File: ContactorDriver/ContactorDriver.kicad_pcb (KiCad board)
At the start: 2 copper layers, 66 x 100 mm, 40 parts, among them J1 PowerConn, J2 DashboardConn, J3 DashboardConn, J4 ContactorConn, J5 PrechargeConn, J6 PrechargeResistorConn, J7 PrechargeResistor, J8 PrechargeResistor, Q1 NTR4003NT1G, Q2 NTR4003NT1G, Q3 CSD18511KTT, Q4 CSD18511KTT

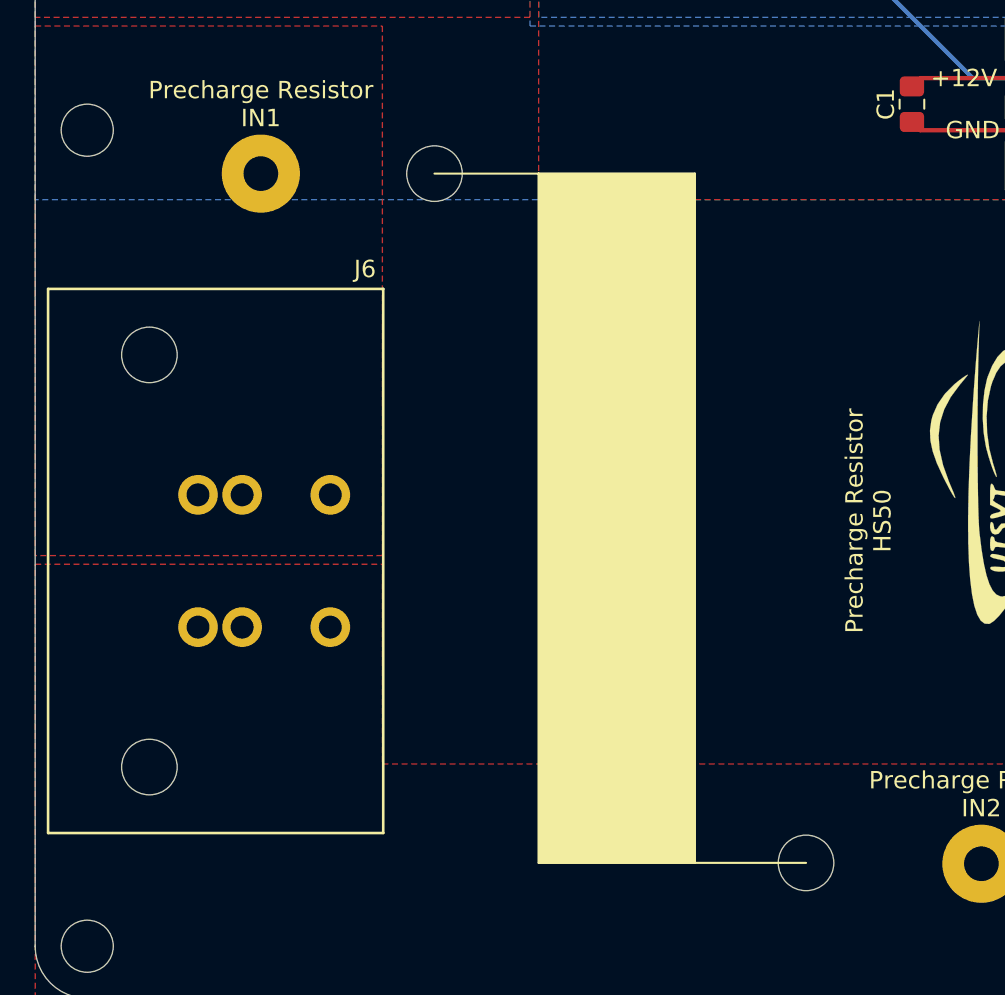
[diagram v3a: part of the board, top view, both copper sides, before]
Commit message: Adds hole dimenions silkscreen text for contactor driver board.
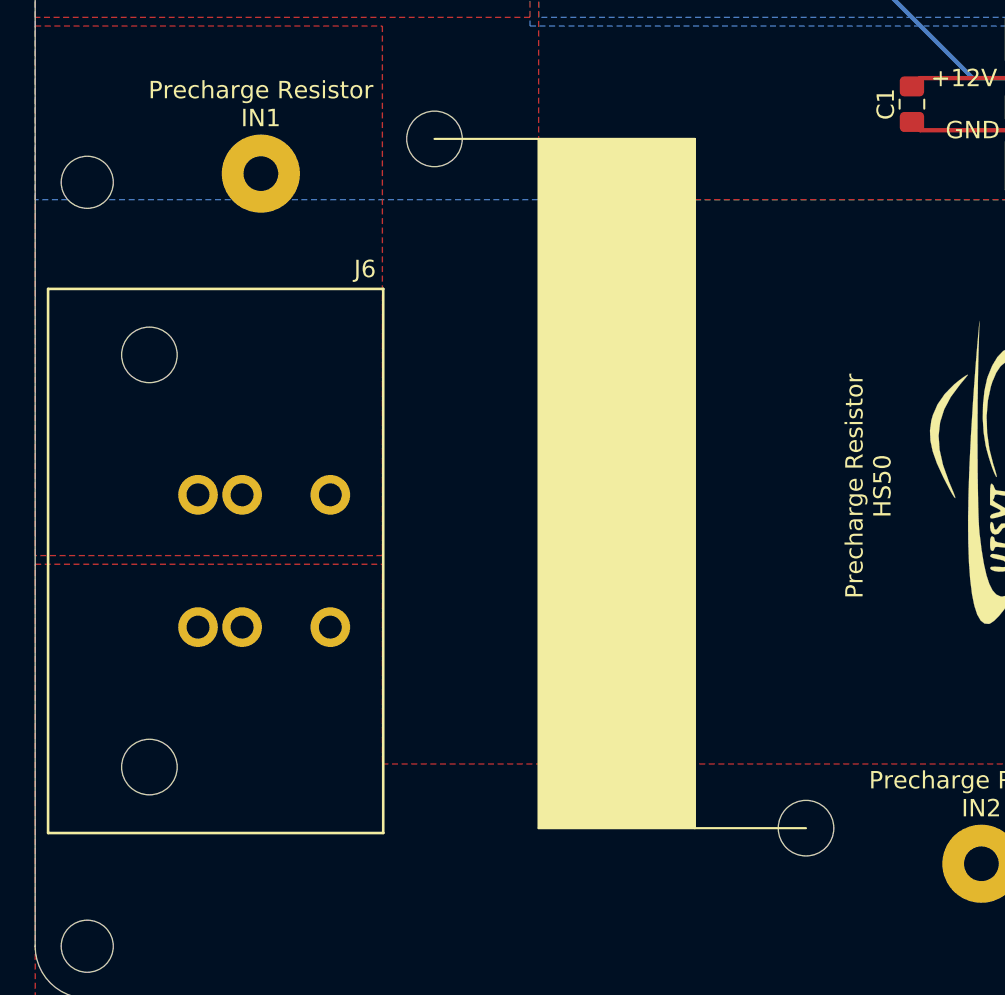
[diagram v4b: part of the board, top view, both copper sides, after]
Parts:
- moved H7 3.00 mm to (167.0, 121.0)
- moved G*** 2.00 mm to (199.0, 132.0)
- moved H1 2.00 mm to (208.4, 158.2)
- moved H2 2.00 mm to (187.0, 118.5)
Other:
- board text added: "44mm"
- board text added: "50mm"
- board text added: "M3"
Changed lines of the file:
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@@
   (general
     (thickness 1.6)
-    (drawings 69)
+    (drawings 81)
     (tracks 61)
     (zones 0)
@@
   )
   (module UTSVT_Special:Hallock_Image (layer B.Cu)
-    (at 199 134 180)
+    (at 199 132 180)
     (fp_text reference G*** (at 0 0) (layer B.SilkS) hide
       (effects (font (size 1.524 1.524) (thickness 0.3)) (justify mirror))
@@
   )
   (module MountingHole:MountingHole_3mm (layer F.Cu)
-    (at 167 118)
+    (at 167 121)
     (descr "Mounting Hole 3mm, no annular")
     (tags "mounting hole 3mm no annular")
@@
   )
   (module MountingHole:MountingHole_3.2mm_M3 (layer F.Cu)
-    (at 208.4 160.2 180)
+    (at 208.4 158.2 180)
     (descr "Mounting Hole 3.2mm, no annular, M3")
     (tags "mounting hole 3.2mm no annular m3")
@@
   )
   (module MountingHole:MountingHole_3.2mm_M3 (layer F.Cu)
-    (at 187 120.5 180)
+    (at 187 118.5 180)
     (descr "Mounting Hole 3.2mm, no annular, M3")
     (tags "mounting hole 3.2mm no annular m3")
@@
       (net 17 "Net-(J6-Pad2)"))
   )
+  (gr_text M3 (at 167 74.75) (layer B.SilkS)
+    (effects (font (size 1 1) (thickness 0.15)) (justify mirror))
+  )
+  (gr_poly (pts (xy 165 71.5) (xy 164.5 71.5) (xy 164.75 71)) (layer B.SilkS) (width 0.1))
+  (gr_line (start 164.5 71) (end 165 71) (layer B.SilkS) (width 0.12))
+  (gr_line (start 164.75 93.5) (end 164.75 71.5) (layer B.SilkS) (width 0.12))
+  (gr_line (start 164.75 120.5) (end 164.75 98.5) (layer B.SilkS) (width 0.12))
+  (gr_text 50mm (at 165 96 270) (layer B.SilkS)
+    (effects (font (size 1 1) (thickness 0.15)) (justify mirror))
+  )
+  (gr_line (start 164.75 140.5) (end 164.75 121.5) (layer B.SilkS) (width 0.12))
+  (gr_line (start 164.75 164.5) (end 164.75 145.5) (layer B.SilkS) (width 0.12))
+  (gr_text 44mm (at 165 143 270) (layer B.SilkS)
+    (effects (font (size 1 1) (thickness 0.15)) (justify mirror))
+  )
+  (gr_line (start 165 121) (end 164.5 121) (layer B.SilkS) (width 0.12))
+  (gr_poly (pts (xy 164.75 121) (xy 164.5 120.5) (xy 165 120.5)) (layer B.SilkS) (width 0.1))
+  (gr_poly (pts (xy 165 121.5) (xy 164.5 121.5) (xy 164.75 121)) (layer B.SilkS) (width 0.1))
   (gr_poly (pts (xy 164.75 165) (xy 164.5 164.5) (xy 165 164.5)) (layer B.SilkS) (width 0.1))
   (gr_line (start 165 165) (end 164.5 165) (layer B.SilkS) (width 0.12))
@@
     (effects (font (size 1 1) (thickness 0.15)))
   )
-  (gr_text "Dr. Gary Hallock" (at 200 152) (layer B.SilkS)
+  (gr_text "Dr. Gary Hallock" (at 200 150) (layer B.SilkS)
     (effects (font (size 1 1) (thickness 0.15)) (justify mirror))
   )
@@
     (effects (font (size 1 1) (thickness 0.15)))
   )
-  (gr_text "Precharge Resistor\nHS50" (at 212 140.5 90) (layer F.SilkS)
+  (gr_text "Precharge Resistor\nHS50" (at 212 138.5 90) (layer F.SilkS)
     (effects (font (size 1 1) (thickness 0.15)))
   )
@@
   (gr_line (start 227 68) (end 167 68) (layer Edge.Cuts) (width 0.05))
   (gr_line (start 230 165) (end 230 71) (layer Edge.Cuts) (width 0.05))
-  (gr_poly (pts (xy 202 120.5) (xy 202 160.2) (xy 193 160.2) (xy 193 120.5)) (layer F.SilkS) (width 0.1))
-  (gr_line (start 193 160.2) (end 202 160.2) (layer F.SilkS) (width 0.12))
-  (gr_line (start 202 120.5) (end 193 120.5) (layer F.SilkS) (width 0.12))
-  (gr_line (start 202 160.2) (end 202 120.5) (layer F.SilkS) (width 0.12))
-  (gr_line (start 193 120.5) (end 193 160.2) (layer F.SilkS) (width 0.12))
-  (gr_line (start 208.4 160.2) (end 202 160.2) (layer F.SilkS) (width 0.12))
-  (gr_line (start 187 120.5) (end 193 120.5) (layer F.SilkS) (width 0.12))
+  (gr_poly (pts (xy 202 118.5) (xy 202 158.2) (xy 193 158.2) (xy 193 118.5)) (layer F.SilkS) (width 0.1))
+  (gr_line (start 193 158.2) (end 202 158.2) (layer F.SilkS) (width 0.12))
+  (gr_line (start 202 118.5) (end 193 118.5) (layer F.SilkS) (width 0.12))
+  (gr_line (start 202 158.2) (end 202 118.5) (layer F.SilkS) (width 0.12))
+  (gr_line (start 193 118.5) (end 193 158.2) (layer F.SilkS) (width 0.12))
+  (gr_line (start 208.4 158.2) (end 202 158.2) (layer F.SilkS) (width 0.12))
+  (gr_line (start 187 118.5) (end 193 118.5) (layer F.SilkS) (width 0.12))
   (segment (start 208 97.475) (end 215 97.475) (width 0.25) (layer F.Cu) (net 1))
   (segment (start 207.1 107.5) (end 208 106.6) (width 0.25) (layer F.Cu) (net 1))
